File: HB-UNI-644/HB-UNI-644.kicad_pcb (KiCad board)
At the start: 2 copper layers, 79 x 78 mm, 51 parts, among them J1 FTDI, J10 ICSP, J11 RAW, J12 Conn_Gnd, J13 Conn_NTC, J2 GS2, J3 I2C_1, J4 GS2, J5 I2C_2, J6 I2C_3, J7 I2C_4, J8 Conn_A, J9 Conn_B, Q1 IRLML6244/IRLML0030, SW1 CONFIG, U1 ATMEGA644PA-AU, U2 CC1101, U3 MAX1724, U4 LM3480-3.3, Y1 8MHz

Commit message: Revision 2 of HB-UNI-644
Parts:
- removed the REF** at (160.0, 152.0)
- removed the REF** at (102.2, 97.2)
- added C15: 1000uF, Capacitors_THT:CP_Radial_D8.0mm_P3.50mm, F.Cu at (86.4, 126.4)
- added C16: 10uF, Capacitors_SMD:C_0805_HandSoldering, B.Cu at (85.1, 97.2)
- added C17: 10nF, Capacitors_SMD:C_0805_HandSoldering, B.Cu at (82.5, 97.2)
- added C18: 10uF, Capacitors_SMD:C_0805_HandSoldering, B.Cu at (92.7, 104.8)
- added C19: 10uF, Capacitors_SMD:C_0805_HandSoldering, B.Cu at (83.8, 104.8)
- added C20: 10nF, Capacitors_SMD:C_0805_HandSoldering, B.Cu at (85.1, 89.5)
- added C21: 10nF, Capacitors_SMD:C_0805_HandSoldering, B.Cu at (95.2, 95.2)
- added F1: *, Resistors_SMD:R_1206_HandSoldering, B.Cu at (114.3, 144.8)
- added Q2: IRLML5203, TO_SOT_Packages_SMD:SOT-23_Handsoldering, B.Cu at (114.9, 141.0)
- added Q3: IRF4905S, TO_SOT_Packages_SMD:TO-263-2, F.Cu at (142.9, 122.6)
- added R11: 100K, Resistors_SMD:R_0805_HandSoldering, B.Cu at (109.2, 143.5)
- added R12: 100K, Resistors_SMD:R_0805_HandSoldering, F.Cu at (132.7, 127.0)
- added REF**: MountingHole_2.2mm_M2_Pad_Via, Mounting_Holes:MountingHole_2.2mm_M2_Pad_Via, F.Cu at (86.5, 79.0)
- added REF**: MountingHole_2.2mm_M2_Pad_Via, Mounting_Holes:MountingHole_2.2mm_M2_Pad_Via, F.Cu at (120.5, 79.0)
- added REF**: MountingHole_2.2mm_M2_Pad_Via, Mounting_Holes:MountingHole_2.2mm_M2_Pad_Via, F.Cu at (154.5, 79.0)
- added REF**: MountingHole_2.2mm_M2_Pad_Via, Mounting_Holes:MountingHole_2.2mm_M2_Pad_Via, F.Cu at (86.5, 147.0)
- added REF**: MountingHole_2.2mm_M2_Pad_Via, Mounting_Holes:MountingHole_2.2mm_M2_Pad_Via, F.Cu at (120.5, 147.0)
- added REF**: MountingHole_2.2mm_M2_Pad_Via, Mounting_Holes:MountingHole_2.2mm_M2_Pad_Via, F.Cu at (154.5, 147.0)
- added U5: CC1101, Homebrew:CC1101, F.Cu at (81.3, 103.5)
- added U6: LM3480-3.3, TO_SOT_Packages_SMD:SOT-23, B.Cu at (88.3, 104.1)
- added U7: TXS0108EPWR, Housings_SSOP:TSSOP-20_4.4x6.5mm_Pitch0.65mm, B.Cu at (90.8, 88.9)
- C12, C9: footprint Capacitors_SMD:C_1206_HandSoldering -> Capacitors_SMD:C_0805_HandSoldering
- D2: value ZMM16V -> ZMM16; moved to F.Cu
- J12: value Conn_Gnd -> Conn_01x04; footprint Pin_Headers:Pin_Header_Straight_1x01_Pitch2.54mm -> Pin_Headers:Pin_Header_Straight_1x04_Pitch2.54mm
- J8, J9: footprint Pin_Headers:Pin_Header_Straight_2x08_Pitch2.54mm -> Pin_Headers:Pin_Header_Straight_2x09_Pitch2.54mm
- Q1: value IRLML6244/IRLML0030 -> IRLML6244
- U4: value LM3480-3.3 -> HT7533-1; footprint TO_SOT_Packages_SMD:SOT-23_Handsoldering -> TO_SOT_Packages_SMD:SOT-89-3_Handsoldering
- Y1: value 8MHz -> 8MHz/16MHz
- moved D2 39.9 mm to (132.7, 118.7), turned to 270 degrees
- moved J12 28.9 mm to (146.7, 108.6), turned to 270 degrees
- moved C11 25.9 mm to (112.4, 128.9), turned to 90 degrees
- moved C14 24.3 mm to (105.4, 99.1)
- moved C13 24.3 mm to (105.4, 96.5)
- moved U2 23.9 mm to (102.9, 99.1), turned to 180 degrees
- moved U4 22.3 mm to (112.4, 135.9), turned to 0 degrees
- moved C9 21.0 mm to (88.3, 134.0)
- moved U3 21.0 mm to (93.3, 136.5)
- moved L1 20.4 mm to (92.7, 141.6)
- moved C10 20.4 mm to (94.0, 132.1)
- moved R4 19.2 mm to (106.7, 144.8), turned to 90 degrees
- moved C12 18.1 mm to (108.6, 128.9), turned to 90 degrees
- moved J2 17.2 mm to (109.9, 149.2)
- moved Q1 12.9 mm to (103.5, 144.8), turned to 90 degrees
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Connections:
- C1 pad 2: +3V3 -> VCC
- C10 pad 1: +3V3 -> VCC
- C11 pad 1: /RAW+ -> Net-(C11-Pad1)
- C12 pad 1: +3V3 -> VCC
- C13 pad 2: +3V3 -> VCC
- C14 pad 2: +3V3 -> VCC
- C2 pad 2: +3V3 -> VCC
- C3 pad 2: +3V3 -> VCC
- C4 pad 2: +3V3 -> VCC
- C9 pad 1: /RAW+ -> /RAW+FUSE
- D2 pad 2: GND -> Net-(D2-Pad2)
- J1 pad 4: +3V3 -> VCC
- J10 pad 2: +3V3 -> VCC
- J12 pad 1: GND -> VCC
- J3 pad 1: +3V3 -> VCC
- J4 pad 1: +3V3 -> VCC
- J5 pad 1: +3V3 -> VCC
- J6 pad 1: +3V3 -> VCC
- J7 pad 1: +3V3 -> VCC
- J8 pad 10: /A4 -> /A3
- J8 pad 12: /A5 -> /A4
- J8 pad 14: /A6 -> /A5
- J8 pad 16: /D3 -> /A6
- J8 pad 2: /A0 -> VCC
- J8 pad 4: /A1 -> /A0
- J8 pad 6: /A2 -> /A1
- J8 pad 8: /A3 -> /A2
- J9 pad 10: /D26 -> /D25
- J9 pad 12: /D27 -> /D26
- J9 pad 14: /D28 -> /D27
- J9 pad 16: /D29 -> /D28
- J9 pad 2: /D30 -> VCC
- J9 pad 4: /D9 -> /D30
- J9 pad 6: /D24 -> /D9
- J9 pad 8: /D25 -> /D24
- L1 pad 1: /RAW+ -> /RAW+FUSE
- Q1 pad 1: Net-(D2-Pad1) -> Net-(Q1-Pad1)
- R1 pad 1: +3V3 -> VCC
- R4 pad 1: /RAW+ -> Net-(Q1-Pad1)
- R4 pad 2: Net-(D2-Pad1) -> /RAW+FUSE
- R5 pad 2: /RAW+ -> /RAW+FUSE
- R7 pad 1: +3V3 -> VCC
- R8 pad 1: +3V3 -> VCC
- U1 pad 17: +3V3 -> VCC
- U1 pad 27: +3V3 -> VCC
- U1 pad 38: +3V3 -> VCC
- U1 pad 5: +3V3 -> VCC
- U2 pad 1: +3V3 -> VCC
- U3 pad 1: /RAW+ -> /RAW+FUSE
- U3 pad 3: /RAW+ -> /RAW+FUSE
- U3 pad 4: +3V3 -> VCC
- U4 pad 1: +3V3 -> GND
- U4 pad 2: /RAW+ -> Net-(C11-Pad1)
- U4 pad 3: GND -> VCC
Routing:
- net VCC: track 0.00 -> 320.9 mm, vias 0 -> 1
- net +3V3: track 230.4 -> 32.9 mm
- net /RAW+FUSE: track 0.00 -> 132.8 mm, vias 0 -> 2
- net GND: track 117.9 -> 195.6 mm, vias 20 -> 28
- net /RAW+: track 135.1 -> 57.5 mm
- net Net-(U5-Pad8): track 0.00 -> 21.9 mm
- net Net-(D2-Pad1): track 18.3 -> 40.0 mm
- net Net-(U5-Pad7): track 0.00 -> 19.7 mm
- net Net-(U5-Pad5): track 0.00 -> 15.6 mm
- net Net-(U5-Pad4): track 0.00 -> 14.9 mm
- net Net-(U5-Pad3): track 0.00 -> 14.6 mm
- net /RSET: track 104.8 -> 118.4 mm, vias 2 -> 3
- net /SS: track 17.9 -> 31.3 mm, vias 2 -> 1
- net Net-(D2-Pad2): track 0.00 -> 12.9 mm
- net /D2: track 30.8 -> 42.7 mm, vias 2 -> 3
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- added copper zone on B.Cu, net /RAW+FUSE
- added copper zone on B.Cu, net Net-(C11-Pad1)
- added copper zone on F.Cu, net Net-(D2-Pad1)
- added copper zone on B.Cu, net VCC
- removed copper zone on B.Cu, net +3V3
- removed copper zone on B.Cu, net /RAW+
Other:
- outline, holes or cut-outs redrawn
- board text added: "4"
- board text added: "5"
- board text added: "D27"
- board text added: "EN"
- board text added: "IN+"
- board text added: "MP2315"
- board text added: "VD+"
- board text added: "Version 2.0 - 07/2018"
- board text removed: "Version 1.0 - 06/2018"

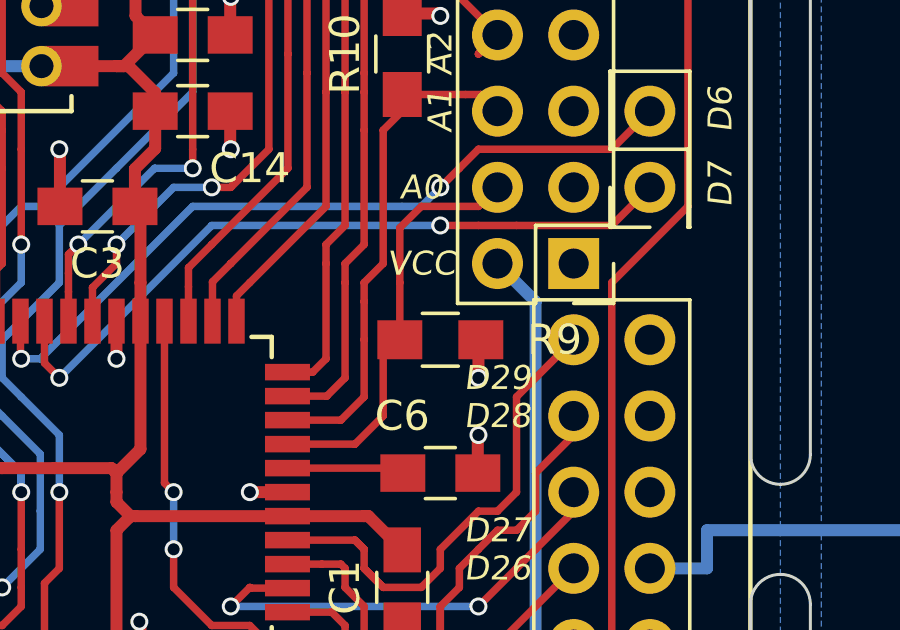
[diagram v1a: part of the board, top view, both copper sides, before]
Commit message: Fixed Gerber files of HB-UNI-SEN-BATT (fixes #2)
Fixed README of HB-UNI-BATT (fixes #1)
Optimized Silkscreen of HB-UNI-644
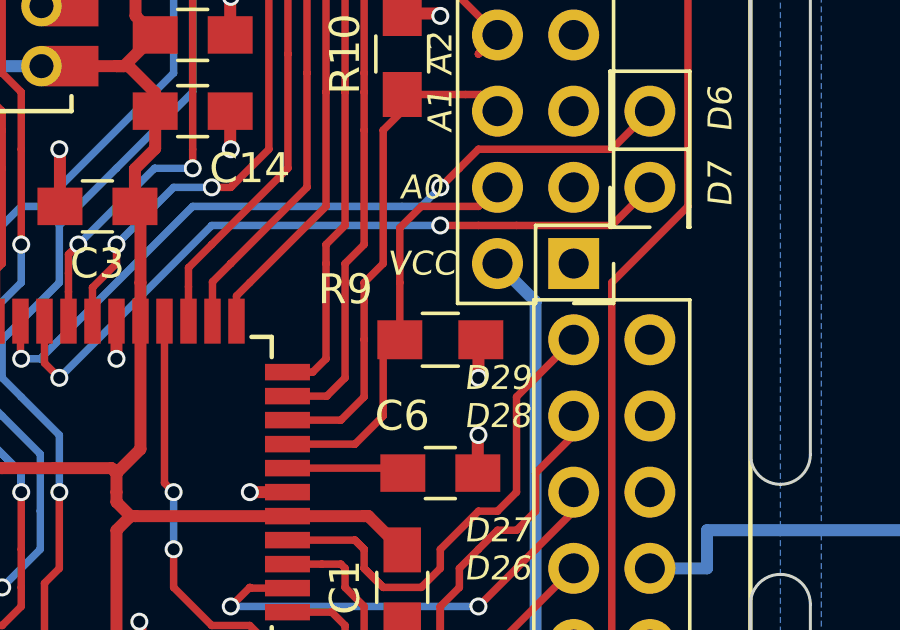
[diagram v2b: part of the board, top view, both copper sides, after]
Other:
- board text added: "Version 2.1 - 07/2018"
- board text removed: "Version 2.0 - 07/2018"
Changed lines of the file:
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@@
       (plotinvisibletext false)
       (padsonsilk false)
-      (subtractmaskfromsilk false)
+      (subtractmaskfromsilk true)
       (outputformat 1)
       (mirror false)
@@
     (tags "resistor 0805")
     (attr smd)
-    (fp_text reference R9 (at -3.81 0 180) (layer F.SilkS)
+    (fp_text reference R9 (at 3.165 1.68 180) (layer F.SilkS)
       (effects (font (size 1 1) (thickness 0.15)))
     )
@@
     (effects (font (size 1.2 1.2) (thickness 0.2)) (justify right mirror))
   )
-  (gr_text "Version 2.0 - 07/2018\n" (at 88.9 111.76) (layer B.SilkS)
+  (gr_text "Version 2.1 - 07/2018\n" (at 88.9 111.76) (layer B.SilkS)
     (effects (font (size 1.2 1.2) (thickness 0.2)) (justify right mirror))
   )

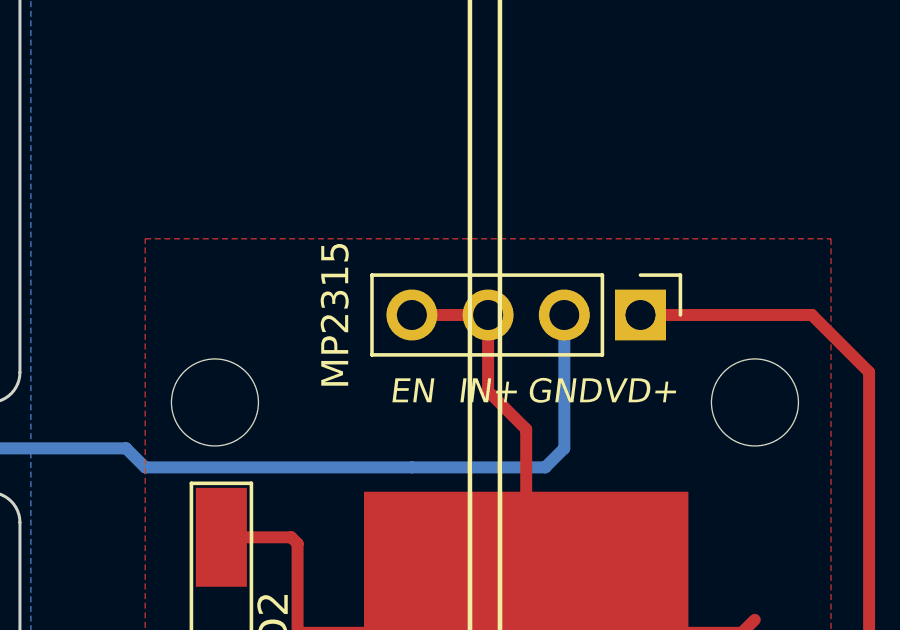
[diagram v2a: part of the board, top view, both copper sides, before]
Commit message: Fixed Stepdown module on HB-UNI-644
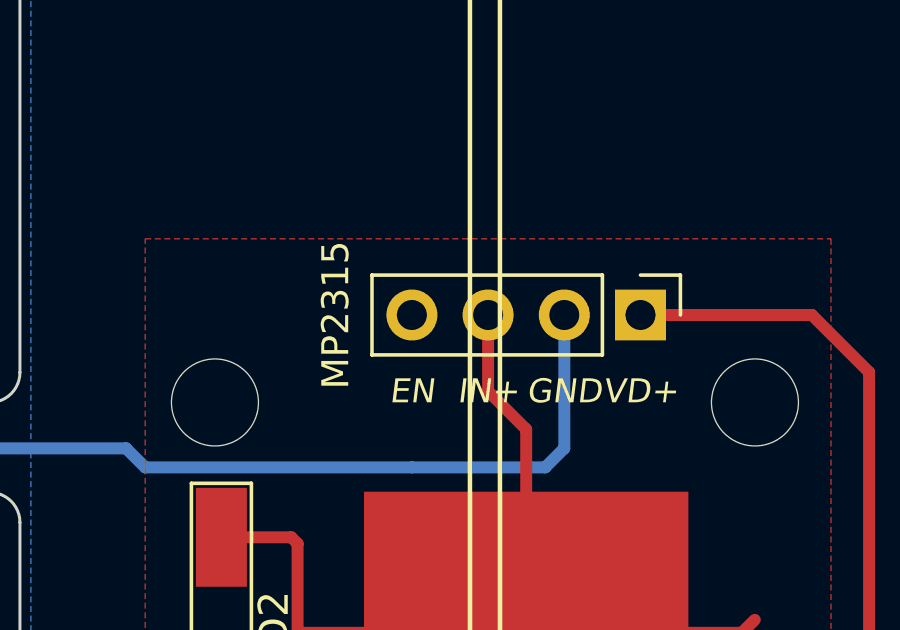
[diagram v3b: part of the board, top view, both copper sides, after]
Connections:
- J12 pad 4: Net-(D2-Pad1) -> Net-(J12-Pad4)
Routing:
- net Net-(D2-Pad1): track 40.0 -> 37.4 mm
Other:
- board text added: "Version 2.2 - 07/2018"
- board text removed: "Version 2.1 - 07/2018"
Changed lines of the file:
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@@
 (kicad_pcb (version 4) (host pcbnew 4.0.7)
   (general
-    (links 214)
+    (links 213)
     (no_connects 0)
     (area 80.949999 73.949999 160.050001 152.050001)
     (thickness 1.6)
     (drawings 104)
-    (tracks 1053)
+    (tracks 1052)
     (zones 0)
     (modules 70)
-    (nets 66)
+    (nets 67)
   )
   (page A4)
@@
   (net 64 "Net-(U7-Pad15)")
   (net 65 "Net-(U7-Pad20)")
+  (net 66 "Net-(J12-Pad4)")
   (net_class Default "Dies ist die voreingestellte Netzklasse."
     (clearance 0.2)
@@
     (add_net "Net-(D1-Pad1)")
     (add_net "Net-(D1-Pad3)")
+    (add_net "Net-(J12-Pad4)")
     (add_net "Net-(L1-Pad2)")
     (add_net "Net-(Q1-Pad1)")
@@
       (net 51 "Net-(D2-Pad1)"))
     (pad 4 thru_hole oval (at 0 7.62 270) (size 1.7 1.7) (drill 1) (layers *.Cu *.Mask)
-      (net 51 "Net-(D2-Pad1)"))
+      (net 66 "Net-(J12-Pad4)"))
     (model ${KISYS3DMOD}/Pin_Headers.3dshapes/Pin_Header_Straight_1x04_Pitch2.54mm.wrl
       (at (xyz 0 0 0))
@@
     (effects (font (size 1.2 1.2) (thickness 0.2)) (justify right mirror))
   )
-  (gr_text "Version 2.1 - 07/2018\n" (at 88.9 111.76) (layer B.SilkS)
+  (gr_text "Version 2.2 - 07/2018\n" (at 88.9 111.76) (layer B.SilkS)
     (effects (font (size 1.2 1.2) (thickness 0.2)) (justify right mirror))
   )
@@
   (segment (start 150.06 119.18) (end 150.495 118.745) (width 0.4) (layer F.Cu) (net 51))
   (segment (start 142.875 119.18) (end 135.255 119.18) (width 0.4) (layer F.Cu) (net 51))
-  (segment (start 139.065 108.585) (end 141.605 108.585) (width 0.4) (layer F.Cu) (net 51))
   (segment (start 141.605 108.585) (end 141.605 111.125) (width 0.4) (layer F.Cu) (net 51))
   (segment (start 142.875 112.395) (end 142.875 119.18) (width 0.4) (layer F.Cu) (net 51))

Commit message: Relicened under CC BY-ND-SA
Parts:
- added G***: LOGO, Homebrew:CC-BY-ND-SA, B.Cu at (110.5, 76.8)
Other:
- board text added: "Version 2.3 - 08/2018"
- board text removed: "Version 2.2 - 07/2018"

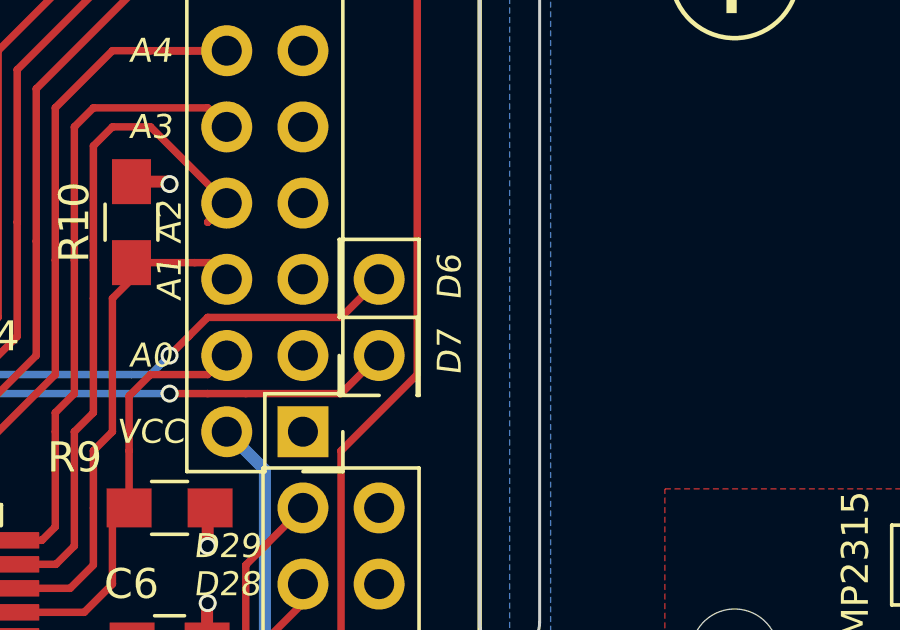
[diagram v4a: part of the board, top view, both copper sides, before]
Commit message: Fixed Silkscreen of D6 and D7 on HB-UNI-644
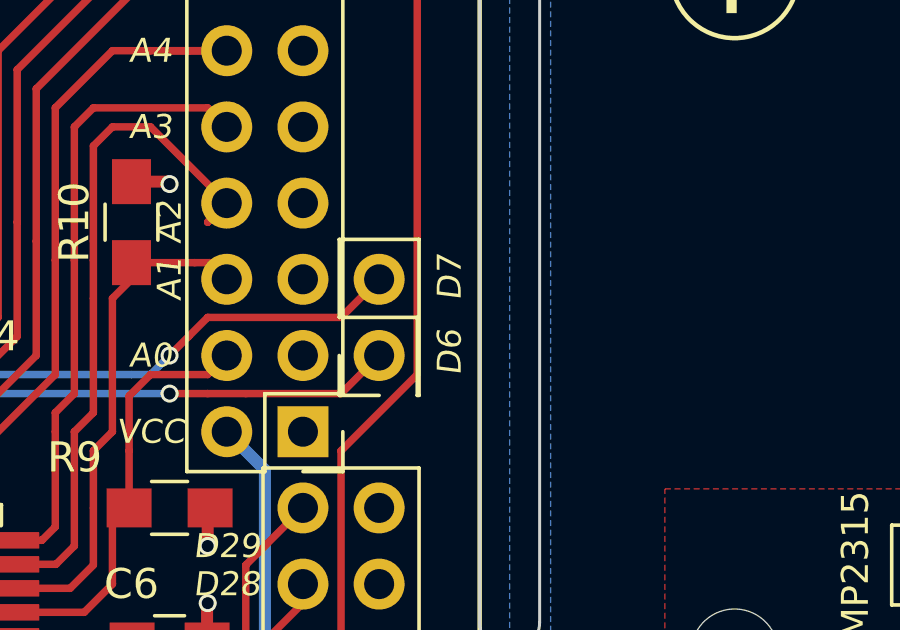
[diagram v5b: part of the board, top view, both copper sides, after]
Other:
- board text added: "Version 2.4 - 08/2018"
- board text removed: "Version 2.3 - 08/2018"
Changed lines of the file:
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@@
     (links 213)
     (no_connects 0)
-    (area 80.949999 73.949999 160.050001 152.050001)
+    (area 73.657143 73.949999 167.342858 152.205)
     (thickness 1.6)
     (drawings 104)
@@
     (effects (font (size 1.2 1.2) (thickness 0.2)) (justify right mirror))
   )
-  (gr_text "Version 2.3 - 08/2018\n" (at 88.9 111.76) (layer B.SilkS)
+  (gr_text "Version 2.4 - 08/2018\n" (at 88.9 111.76) (layer B.SilkS)
     (effects (font (size 1.2 1.2) (thickness 0.2)) (justify right mirror))
   )
@@
     (effects (font (size 0.8 0.8) (thickness 0.15) italic))
   )
-  (gr_text D7 (at 123 101.5 90) (layer F.SilkS)
+  (gr_text D7 (at 123 99 90) (layer F.SilkS)
     (effects (font (size 0.8 0.8) (thickness 0.15) italic))
   )
-  (gr_text D6 (at 123 99 90) (layer F.SilkS)
+  (gr_text D6 (at 123 101.5 90) (layer F.SilkS)
     (effects (font (size 0.8 0.8) (thickness 0.15) italic))
   )

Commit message: Added HB-RF-USB
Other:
- rule solder_mask_min_width: 0.25 -> 0.15
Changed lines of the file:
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@@
     (pad_drill 0)
     (pad_to_mask_clearance 0)
-    (solder_mask_min_width 0.25)
+    (solder_mask_min_width 0.15)
     (aux_axis_origin 0 0)
-    (visible_elements 7FFEFF7F)
+    (visible_elements 7FFFFF7F)
     (pcbplotparams
-      (layerselection 0x010f0_80000001)
+      (layerselection 0x010f0_ffffffff)
       (usegerberextensions false)
-      (usegerberattributes true)
+      (usegerberattributes false)
       (usegerberadvancedattributes false)
       (creategerberjobfile false)
